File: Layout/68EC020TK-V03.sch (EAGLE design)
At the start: 101 parts, among them IC10 74HCT245PW, IC11 74HCT245PW, IC12 AM29F010S, IC13 XC95288XL-TQ144, IC14 ICS570B, IC15 74HCT245PW, IC2 MC68EC020FG, IC3 74ACT16245, IC4 74ACT16245, IC5 LD117AS33TR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

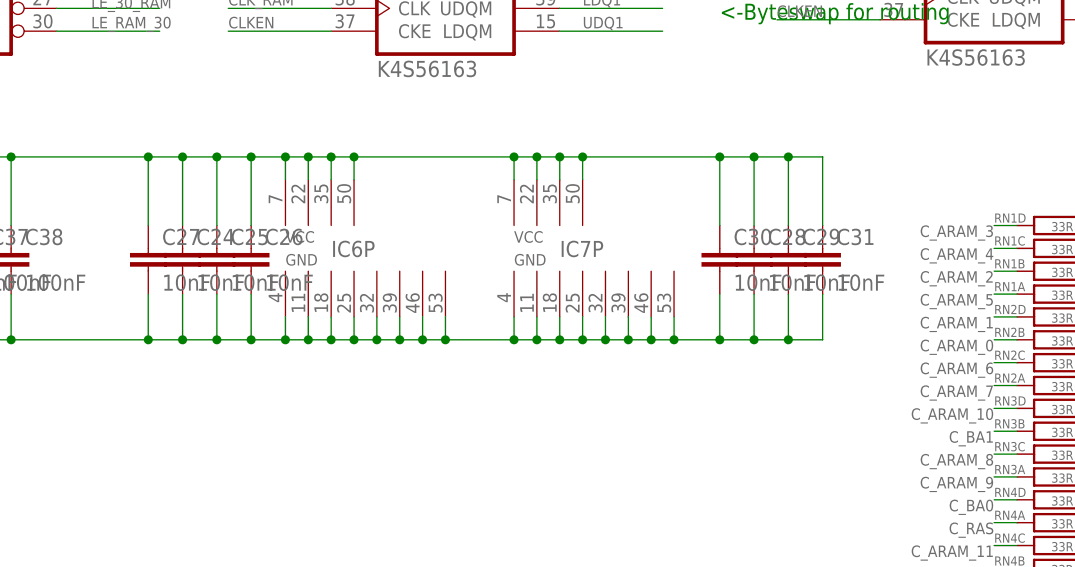
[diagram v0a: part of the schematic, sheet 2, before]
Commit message: Fixed some Packages
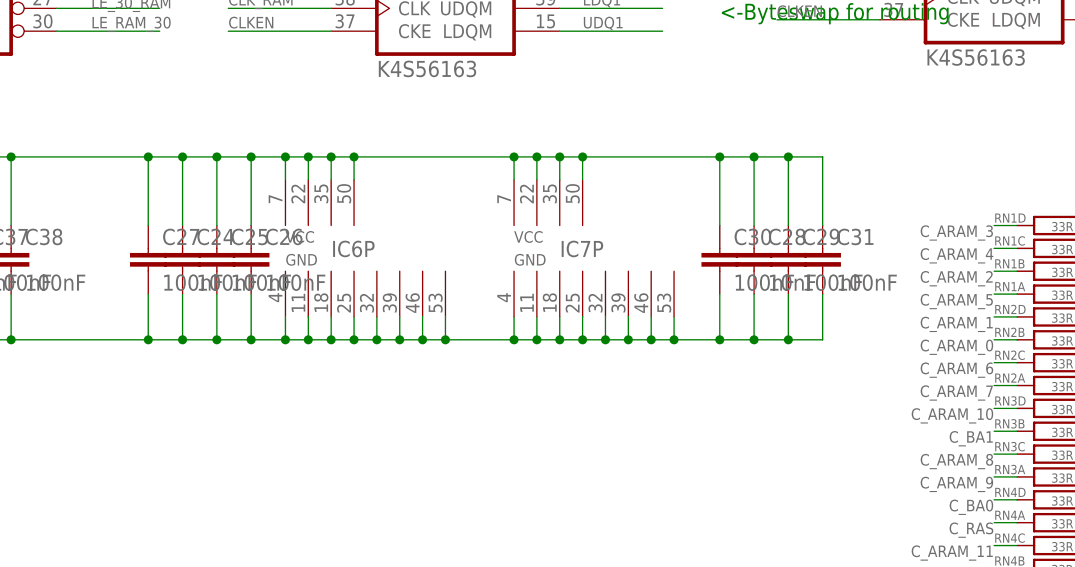
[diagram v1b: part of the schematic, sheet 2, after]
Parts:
- C24, C25, C26, C27, C29, C30, C31: value 10nF -> 100nF
- C39: device rcl:C-EUC0805K -> rcl:C-EUC1206K
- C43, C44: value (none) -> 100nF
- X1: value (none) -> 16,66MHz / 3.3V
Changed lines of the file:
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@@
 <grid distance="0.1" unitdist="inch" unit="inch" style="lines" multiple="1" display="no" altdistance="0.01" altunitdist="inch" altunit="inch"/>
 <layers>
-<layer number="1" name="Top" color="4" fill="1" visible="no" active="no"/>
-<layer number="2" name="Route2" color="1" fill="3" visible="no" active="no"/>
-<layer number="3" name="Route3" color="4" fill="3" visible="no" active="no"/>
-<layer number="14" name="Route14" color="1" fill="6" visible="no" active="no"/>
-<layer number="15" name="Route15" color="4" fill="6" visible="no" active="no"/>
-<layer number="16" name="Bottom" color="1" fill="1" visible="no" active="no"/>
-<layer number="17" name="Pads" color="2" fill="1" visible="no" active="no"/>
-<layer number="18" name="Vias" color="2" fill="1" visible="no" active="no"/>
-<layer number="19" name="Unrouted" color="6" fill="1" visible="no" active="no"/>
-<layer number="20" name="Dimension" color="15" fill="1" visible="no" active="no"/>
-<layer number="21" name="tPlace" color="7" fill="1" visible="no" active="no"/>
-<layer number="22" name="bPlace" color="7" fill="1" visible="no" active="no"/>
-<layer number="23" name="tOrigins" color="15" fill="1" visible="no" active="no"/>
-<layer number="24" name="bOrigins" color="15" fill="1" visible="no" active="no"/>
-<layer number="25" name="tNames" color="7" fill="1" visible="no" active="no"/>
-<layer number="26" name="bNames" color="7" fill="1" visible="no" active="no"/>
-<layer number="27" name="tValues" color="7" fill="1" visible="no" active="no"/>
-<layer number="28" name="bValues" color="7" fill="1" visible="no" active="no"/>
+<layer number="1" name="Top" color="4" fill="1" visible="yes" active="no"/>
+<layer number="2" name="Route2" color="1" fill="3" visible="yes" active="no"/>
+<layer number="3" name="Route3" color="4" fill="3" visible="yes" active="no"/>
+<layer number="14" name="Route14" color="1" fill="6" visible="yes" active="no"/>
+<layer number="15" name="Route15" color="4" fill="6" visible="yes" active="no"/>
+<layer number="16" name="Bottom" color="1" fill="1" visible="yes" active="no"/>
+<layer number="17" name="Pads" color="2" fill="1" visible="yes" active="no"/>
+<layer number="18" name="Vias" color="2" fill="1" visible="yes" active="no"/>
+<layer number="19" name="Unrouted" color="6" fill="1" visible="yes" active="no"/>
+<layer number="20" name="Dimension" color="15" fill="1" visible="yes" active="no"/>
+<layer number="21" name="tPlace" color="7" fill="1" visible="yes" active="no"/>
+<layer number="22" name="bPlace" color="7" fill="1" visible="yes" active="no"/>
+<layer number="23" name="tOrigins" color="15" fill="1" visible="yes" active="no"/>
+<layer number="24" name="bOrigins" color="15" fill="1" visible="yes" active="no"/>
+<layer number="25" name="tNames" color="7" fill="1" visible="yes" active="no"/>
+<layer number="26" name="bNames" color="7" fill="1" visible="yes" active="no"/>
+<layer number="27" name="tValues" color="7" fill="1" visible="yes" active="no"/>
+<layer number="28" name="bValues" color="7" fill="1" visible="yes" active="no"/>
 <layer number="29" name="tStop" color="7" fill="3" visible="no" active="no"/>
 <layer number="30" name="bStop" color="7" fill="6" visible="no" active="no"/>
@@
 <layer number="35" name="tGlue" color="7" fill="4" visible="no" active="no"/>
 <layer number="36" name="bGlue" color="7" fill="5" visible="no" active="no"/>
-<layer number="37" name="tTest" color="7" fill="1" visible="no" active="no"/>
-<layer number="38" name="bTest" color="7" fill="1" visible="no" active="no"/>
+<layer number="37" name="tTest" color="7" fill="1" visible="yes" active="no"/>
+<layer number="38" name="bTest" color="7" fill="1" visible="yes" active="no"/>
 <layer number="39" name="tKeepout" color="4" fill="11" visible="no" active="no"/>
 <layer number="40" name="bKeepout" color="1" fill="11" visible="no" active="no"/>
@@
 <layer number="44" name="Drills" color="7" fill="1" visible="no" active="no"/>
 <layer number="45" name="Holes" color="7" fill="1" visible="no" active="no"/>
-<layer number="46" name="Milling" color="3" fill="1" visible="no" active="no"/>
-<layer number="47" name="Measures" color="7" fill="1" visible="no" active="no"/>
-<layer number="48" name="Document" color="7" fill="1" visible="no" active="no"/>
-<layer number="49" name="Reference" color="7" fill="1" visible="no" active="no"/>
-<layer number="50" name="dxf" color="7" fill="1" visible="no" active="no"/>
-<layer number="51" name="tDocu" color="7" fill="1" visible="no" active="no"/>
-<layer number="52" name="bDocu" color="7" fill="1" visible="no" active="no"/>
+<layer number="46" name="Milling" color="3" fill="1" visible="yes" active="no"/>
+<layer number="47" name="Measures" color="7" fill="1" visible="yes" active="no"/>
+<layer number="48" name="Document" color="7" fill="1" visible="yes" active="no"/>
+<layer number="49" name="Reference" color="7" fill="1" visible="yes" active="no"/>
+<layer number="50" name="dxf" color="7" fill="1" visible="yes" active="no"/>
+<layer number="51" name="tDocu" color="7" fill="1" visible="yes" active="no"/>
+<layer number="52" name="bDocu" color="7" fill="1" visible="yes" active="no"/>
 <layer number="91" name="Nets" color="2" fill="1" visible="yes" active="yes"/>
 <layer number="92" name="Busses" color="1" fill="1" visible="yes" active="yes"/>
@@
 <part name="RN5" library="SMD" deviceset="R-NETZ@3" device="" value="33R"/>
 <part name="RN6" library="SMD" deviceset="R-NETZ@3" device="" value="33R"/>
-<part name="C27" library="rcl" deviceset="C-EU" device="C0603K" value="10nF"/>
-<part name="C24" library="rcl" deviceset="C-EU" device="C0603K" value="10nF"/>
-<part name="C25" library="rcl" deviceset="C-EU" device="C0603K" value="10nF"/>
-<part name="C26" library="rcl" deviceset="C-EU" device="C0603K" value="10nF"/>
-<part name="C30" library="rcl" deviceset="C-EU" device="C0603K" value="10nF"/>
+<part name="C27" library="rcl" deviceset="C-EU" device="C0603K" value="100nF"/>
+<part name="C24" library="rcl" deviceset="C-EU" device="C0603K" value="100nF"/>
+<part name="C25" library="rcl" deviceset="C-EU" device="C0603K" value="100nF"/>
+<part name="C26" library="rcl" deviceset="C-EU" device="C0603K" value="100nF"/>
+<part name="C30" library="rcl" deviceset="C-EU" device="C0603K" value="100nF"/>
 <part name="C28" library="rcl" deviceset="C-EU" device="C0603K" value="10nF"/>
-<part name="C29" library="rcl" deviceset="C-EU" device="C0603K" value="10nF"/>
-<part name="C31" library="rcl" deviceset="C-EU" device="C0603K" value="10nF"/>
+<part name="C29" library="rcl" deviceset="C-EU" device="C0603K" value="100nF"/>
+<part name="C31" library="rcl" deviceset="C-EU" device="C0603K" value="100nF"/>
 <part name="C19" library="rcl" deviceset="C-EU" device="C0603K" value="100nF"/>
 <part name="C20" library="rcl" deviceset="C-EU" device="C0603K" value="100nF"/>
@@
 <part name="R1" library="rcl" deviceset="R-EU_" device="R0603" value="330"/>
 <part name="P+9" library="supply1" deviceset="VCC" device=""/>
-<part name="C39" library="rcl" deviceset="C-EU" device="C0805K" value="47µF"/>
+<part name="C39" library="rcl" deviceset="C-EU" device="C1206K" value="47µF"/>
 <part name="GND13" library="supply1" deviceset="GND" device=""/>
 <part name="C40" library="rcl" deviceset="C-EU" device="C0603K" value="100nF"/>
@@
 <part name="IC10" library="74xx-eu" deviceset="74*245" device="PW" technology="HCT" value="74HCT245PW"/>
 <part name="IC15" library="74xx-eu" deviceset="74*245" device="PW" technology="HCT" value="74HCT245PW"/>
-<part name="X1" library="SMD-Crystal" deviceset="CSX-750FC" device="FC(5V)"/>
-<part name="C43" library="rcl" deviceset="C-EU" device="C0603K"/>
+<part name="X1" library="SMD-Crystal" deviceset="CSX-750FC" device="FC(5V)" value="16,66MHz / 3.3V"/>
+<part name="C43" library="rcl" deviceset="C-EU" device="C0603K" value="100nF"/>
 <part name="+3V12" library="supply1" deviceset="+3V3" device=""/>
 <part name="GND39" library="supply1" deviceset="GND" device=""/>
-<part name="C44" library="rcl" deviceset="C-EU" device="C0603K"/>
+<part name="C44" library="rcl" deviceset="C-EU" device="C0603K" value="100nF"/>
 <part name="FB1" library="rcl" deviceset="R-EU_" device="R0603" value="100Ohm@100MHz"/>
 <part name="R15" library="rcl" deviceset="R-EU_" device="R0603" value="33"/>

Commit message: fixed parts but mem cfg not bug free
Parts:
- C28: value 10nF -> 100nF
- C39: value 47µF -> 47uF
- FB1: value 100Ohm@100MHz -> 120Ohm@100MHz 0.5A
- IC12: value AM29F010S -> AM29F010S-10
- IC13: value XC95288XL-TQ144 -> XC95288XL-TQ144-10ns
- IC6, IC7: value 74ALVT16543 -> 74LVT16543
- IC8, IC9: value K4S56163 -> AS4C4M16SA-6TCN
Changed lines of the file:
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@@
 <grid distance="0.1" unitdist="inch" unit="inch" style="lines" multiple="1" display="no" altdistance="0.01" altunitdist="inch" altunit="inch"/>
 <layers>
-<layer number="1" name="Top" color="4" fill="1" visible="yes" active="no"/>
-<layer number="2" name="Route2" color="1" fill="3" visible="yes" active="no"/>
-<layer number="3" name="Route3" color="4" fill="3" visible="yes" active="no"/>
-<layer number="14" name="Route14" color="1" fill="6" visible="yes" active="no"/>
-<layer number="15" name="Route15" color="4" fill="6" visible="yes" active="no"/>
-<layer number="16" name="Bottom" color="1" fill="1" visible="yes" active="no"/>
-<layer number="17" name="Pads" color="2" fill="1" visible="yes" active="no"/>
-<layer number="18" name="Vias" color="2" fill="1" visible="yes" active="no"/>
-<layer number="19" name="Unrouted" color="6" fill="1" visible="yes" active="no"/>
-<layer number="20" name="Dimension" color="15" fill="1" visible="yes" active="no"/>
-<layer number="21" name="tPlace" color="7" fill="1" visible="yes" active="no"/>
-<layer number="22" name="bPlace" color="7" fill="1" visible="yes" active="no"/>
-<layer number="23" name="tOrigins" color="15" fill="1" visible="yes" active="no"/>
-<layer number="24" name="bOrigins" color="15" fill="1" visible="yes" active="no"/>
-<layer number="25" name="tNames" color="7" fill="1" visible="yes" active="no"/>
-<layer number="26" name="bNames" color="7" fill="1" visible="yes" active="no"/>
-<layer number="27" name="tValues" color="7" fill="1" visible="yes" active="no"/>
-<layer number="28" name="bValues" color="7" fill="1" visible="yes" active="no"/>
+<layer number="1" name="Top" color="4" fill="1" visible="no" active="no"/>
+<layer number="2" name="Route2" color="1" fill="3" visible="no" active="no"/>
+<layer number="3" name="Route3" color="4" fill="3" visible="no" active="no"/>
+<layer number="14" name="Route14" color="1" fill="6" visible="no" active="no"/>
+<layer number="15" name="Route15" color="4" fill="6" visible="no" active="no"/>
+<layer number="16" name="Bottom" color="1" fill="1" visible="no" active="no"/>
+<layer number="17" name="Pads" color="2" fill="1" visible="no" active="no"/>
+<layer number="18" name="Vias" color="2" fill="1" visible="no" active="no"/>
+<layer number="19" name="Unrouted" color="6" fill="1" visible="no" active="no"/>
+<layer number="20" name="Dimension" color="15" fill="1" visible="no" active="no"/>
+<layer number="21" name="tPlace" color="7" fill="1" visible="no" active="no"/>
+<layer number="22" name="bPlace" color="7" fill="1" visible="no" active="no"/>
+<layer number="23" name="tOrigins" color="15" fill="1" visible="no" active="no"/>
+<layer number="24" name="bOrigins" color="15" fill="1" visible="no" active="no"/>
+<layer number="25" name="tNames" color="7" fill="1" visible="no" active="no"/>
+<layer number="26" name="bNames" color="7" fill="1" visible="no" active="no"/>
+<layer number="27" name="tValues" color="7" fill="1" visible="no" active="no"/>
+<layer number="28" name="bValues" color="7" fill="1" visible="no" active="no"/>
 <layer number="29" name="tStop" color="7" fill="3" visible="no" active="no"/>
 <layer number="30" name="bStop" color="7" fill="6" visible="no" active="no"/>
@@
 <layer number="35" name="tGlue" color="7" fill="4" visible="no" active="no"/>
 <layer number="36" name="bGlue" color="7" fill="5" visible="no" active="no"/>
-<layer number="37" name="tTest" color="7" fill="1" visible="yes" active="no"/>
-<layer number="38" name="bTest" color="7" fill="1" visible="yes" active="no"/>
+<layer number="37" name="tTest" color="7" fill="1" visible="no" active="no"/>
+<layer number="38" name="bTest" color="7" fill="1" visible="no" active="no"/>
 <layer number="39" name="tKeepout" color="4" fill="11" visible="no" active="no"/>
 <layer number="40" name="bKeepout" color="1" fill="11" visible="no" active="no"/>
@@
 <layer number="44" name="Drills" color="7" fill="1" visible="no" active="no"/>
 <layer number="45" name="Holes" color="7" fill="1" visible="no" active="no"/>
-<layer number="46" name="Milling" color="3" fill="1" visible="yes" active="no"/>
-<layer number="47" name="Measures" color="7" fill="1" visible="yes" active="no"/>
-<layer number="48" name="Document" color="7" fill="1" visible="yes" active="no"/>
-<layer number="49" name="Reference" color="7" fill="1" visible="yes" active="no"/>
-<layer number="50" name="dxf" color="7" fill="1" visible="yes" active="no"/>
-<layer number="51" name="tDocu" color="7" fill="1" visible="yes" active="no"/>
-<layer number="52" name="bDocu" color="7" fill="1" visible="yes" active="no"/>
+<layer number="46" name="Milling" color="3" fill="1" visible="no" active="no"/>
+<layer number="47" name="Measures" color="7" fill="1" visible="no" active="no"/>
+<layer number="48" name="Document" color="7" fill="1" visible="no" active="no"/>
+<layer number="49" name="Reference" color="7" fill="1" visible="no" active="no"/>
+<layer number="50" name="dxf" color="7" fill="1" visible="no" active="no"/>
+<layer number="51" name="tDocu" color="7" fill="1" visible="no" active="no"/>
+<layer number="52" name="bDocu" color="7" fill="1" visible="no" active="no"/>
 <layer number="91" name="Nets" color="2" fill="1" visible="yes" active="yes"/>
 <layer number="92" name="Busses" color="1" fill="1" visible="yes" active="yes"/>
@@
 <part name="GND8" library="supply1" deviceset="GND" device="" value="GND"/>
 <part name="P+8" library="supply1" deviceset="3,3V" device="" value="3,3V"/>
-<part name="IC8" library="SMD-IC" deviceset="K4S56163@2" device="" value="K4S56163"/>
-<part name="IC9" library="SMD-IC" deviceset="K4S56163@2" device="" value="K4S56163"/>
+<part name="IC8" library="SMD-IC" deviceset="K4S56163@2" device="" value="AS4C4M16SA-6TCN"/>
+<part name="IC9" library="SMD-IC" deviceset="K4S56163@2" device="" value="AS4C4M16SA-6TCN"/>
 <part name="C17" library="rcl" deviceset="C-EU" device="C0603K" value="100nF"/>
 <part name="C18" library="rcl" deviceset="C-EU" device="C0603K" value="100nF"/>
@@
 <part name="GND11" library="supply1" deviceset="GND" device="" value="GND"/>
 <part name="GND12" library="supply1" deviceset="GND" device="" value="GND"/>
-<part name="IC6" library="SMD-IC" deviceset="ABT16543@2" device="" value="74ALVT16543"/>
-<part name="IC7" library="SMD-IC" deviceset="ABT16543@2" device="" value="74ALVT16543"/>
+<part name="IC6" library="SMD-IC" deviceset="ABT16543@2" device="" value="74LVT16543"/>
+<part name="IC7" library="SMD-IC" deviceset="ABT16543@2" device="" value="74LVT16543"/>
 <part name="RN1" library="SMD" deviceset="R-NETZ@3" device="" value="33R"/>
 <part name="RN2" library="SMD" deviceset="R-NETZ@3" device="" value="33R"/>
@@
 <part name="C26" library="rcl" deviceset="C-EU" device="C0603K" value="100nF"/>
 <part name="C30" library="rcl" deviceset="C-EU" device="C0603K" value="100nF"/>
-<part name="C28" library="rcl" deviceset="C-EU" device="C0603K" value="10nF"/>
+<part name="C28" library="rcl" deviceset="C-EU" device="C0603K" value="100nF"/>
 <part name="C29" library="rcl" deviceset="C-EU" device="C0603K" value="100nF"/>
 <part name="C31" library="rcl" deviceset="C-EU" device="C0603K" value="100nF"/>
@@
 <part name="R2" library="rcl" deviceset="R-EU_" device="R0603" value="4.7k"/>
 <part name="F1" library="rcl" deviceset="R-EU_" device="R2512" value="500mA"/>
-<part name="IC12" library="am29-memory" deviceset="AM29F010S" device=""/>
+<part name="IC12" library="am29-memory" deviceset="AM29F010S" device="" value="AM29F010S-10"/>
 <part name="IDE_ACT" library="con-molex" deviceset="22-?-02" device="05-7028"/>
 <part name="R1" library="rcl" deviceset="R-EU_" device="R0603" value="330"/>
 <part name="P+9" library="supply1" deviceset="VCC" device=""/>
-<part name="C39" library="rcl" deviceset="C-EU" device="C1206K" value="47µF"/>
+<part name="C39" library="rcl" deviceset="C-EU" device="C1206K" value="47uF"/>
 <part name="GND13" library="supply1" deviceset="GND" device=""/>
 <part name="C40" library="rcl" deviceset="C-EU" device="C0603K" value="100nF"/>
@@
 <part name="GND14" library="supply1" deviceset="GND" device=""/>
 <part name="P+10" library="supply1" deviceset="VCC" device=""/>
-<part name="IC13" library="xilinx_xc9572xl-tq100" deviceset="XC95288XL-TQ144" device=""/>
+<part name="IC13" library="xilinx_xc9572xl-tq100" deviceset="XC95288XL-TQ144" device="" value="XC95288XL-TQ144-10ns"/>
 <part name="C46" library="rcl" deviceset="C-EU" device="C0603K" value="100nF"/>
 <part name="C47" library="rcl" deviceset="C-EU" device="C0603K" value="100nF"/>
@@
 <part name="GND39" library="supply1" deviceset="GND" device=""/>
 <part name="C44" library="rcl" deviceset="C-EU" device="C0603K" value="100nF"/>
-<part name="FB1" library="rcl" deviceset="R-EU_" device="R0603" value="100Ohm@100MHz"/>
+<part name="FB1" library="rcl" deviceset="R-EU_" device="R0603" value="120Ohm@100MHz 0.5A"/>
 <part name="R15" library="rcl" deviceset="R-EU_" device="R0603" value="33"/>
 <part name="R17" library="rcl" deviceset="R-EU_" device="R0603" value="33"/>

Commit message: Improved layout
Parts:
- added R3, R4: n.b., rcl:R-EU_R0603
- C44: value 100nF -> n.b.
- FB1: value 120Ohm@100MHz 0.5A -> n.b.
- IC14: value ICS570B -> ICS570A
- IC5: value LD117AS33TR -> LD117ADT33TR; device v-reg:LD117AS33TR -> v-reg:LD117ADT33TR
- R15: value 33 -> n.b.
- X1: value 16,66MHz / 3.3V -> n.b.
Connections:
- net +5V: no longer R12.2, R13.2
- net GND: now also R3.1, R4.1
- net S0: now also R4.2
- net S1: now also R3.2
- net VCC_IC14: now also R12.2, R13.2
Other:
- note added: "R3/R4 are populated with 4k7 for a 570B"
- moved on the sheet: C43, IC14, IC14G$2, R10, R11, SJ1, SJ2
